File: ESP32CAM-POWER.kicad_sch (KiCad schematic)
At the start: 20 parts

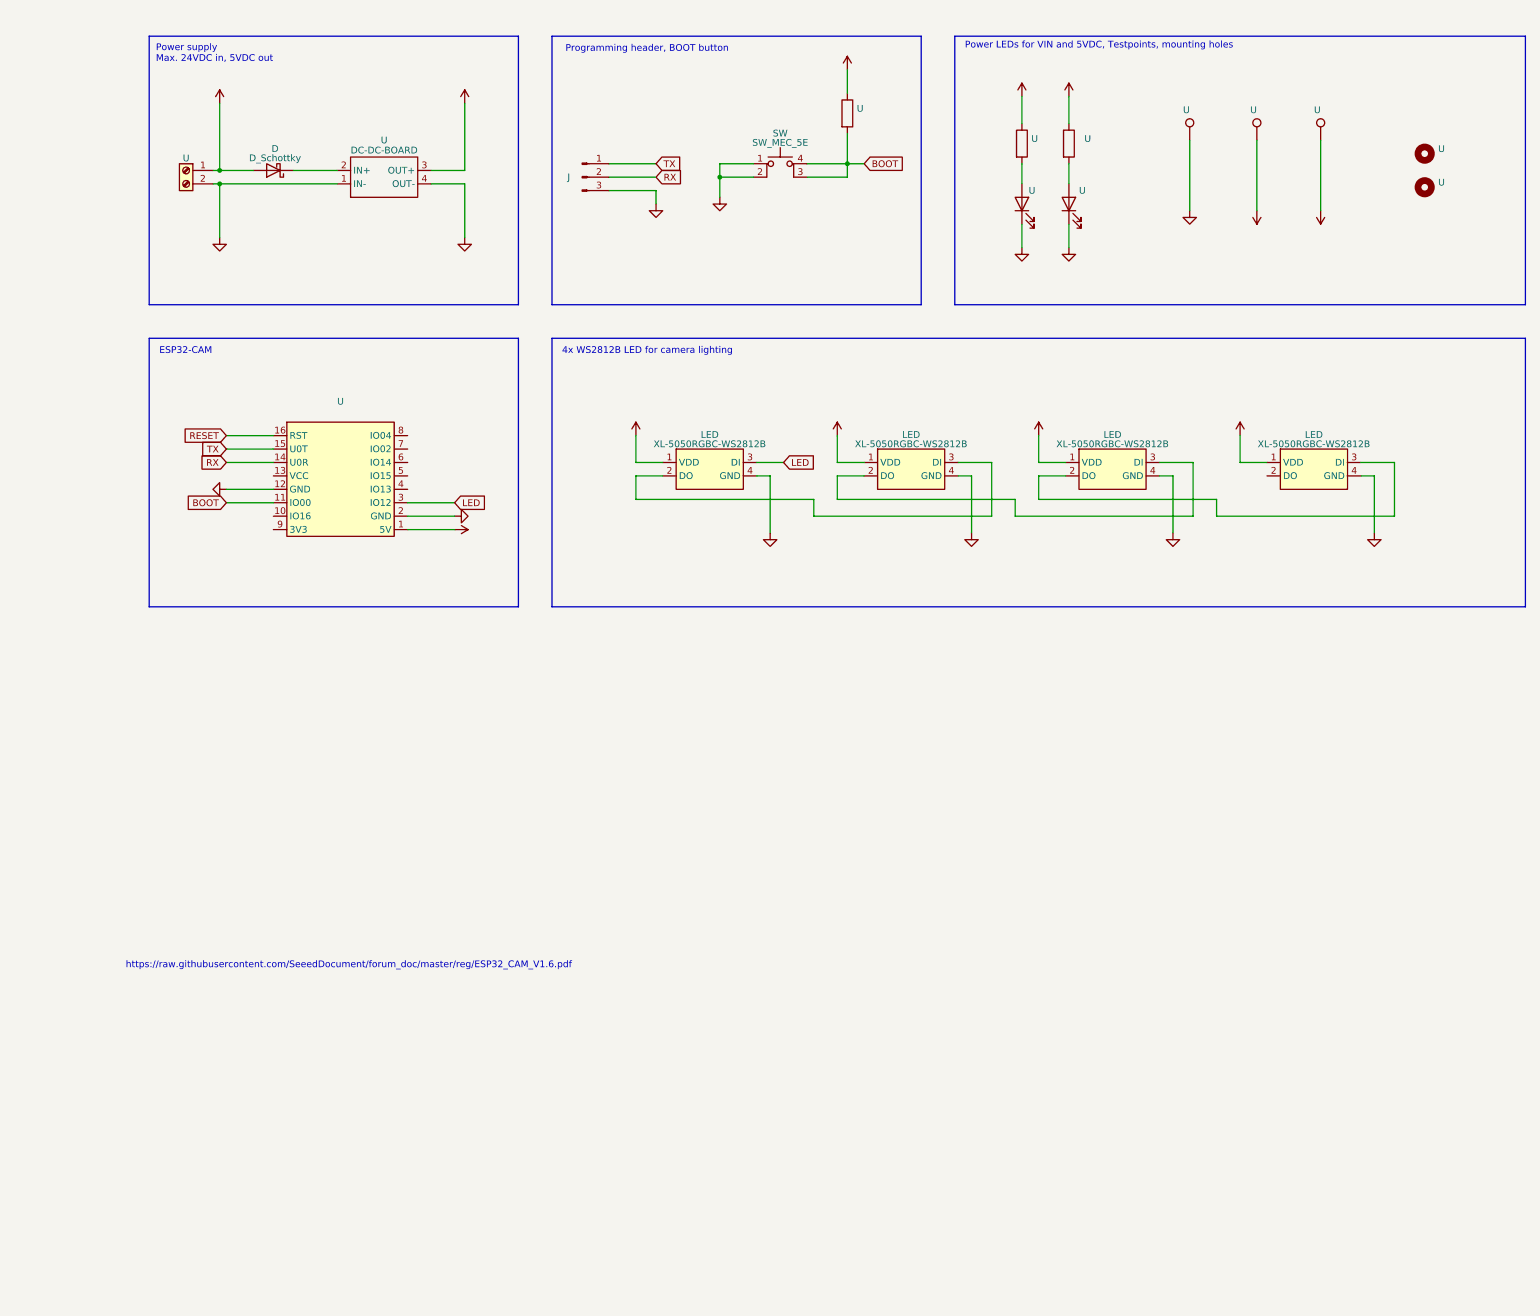
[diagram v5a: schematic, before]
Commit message: fixed several bugs, replaced DCDC Module with onboard step down
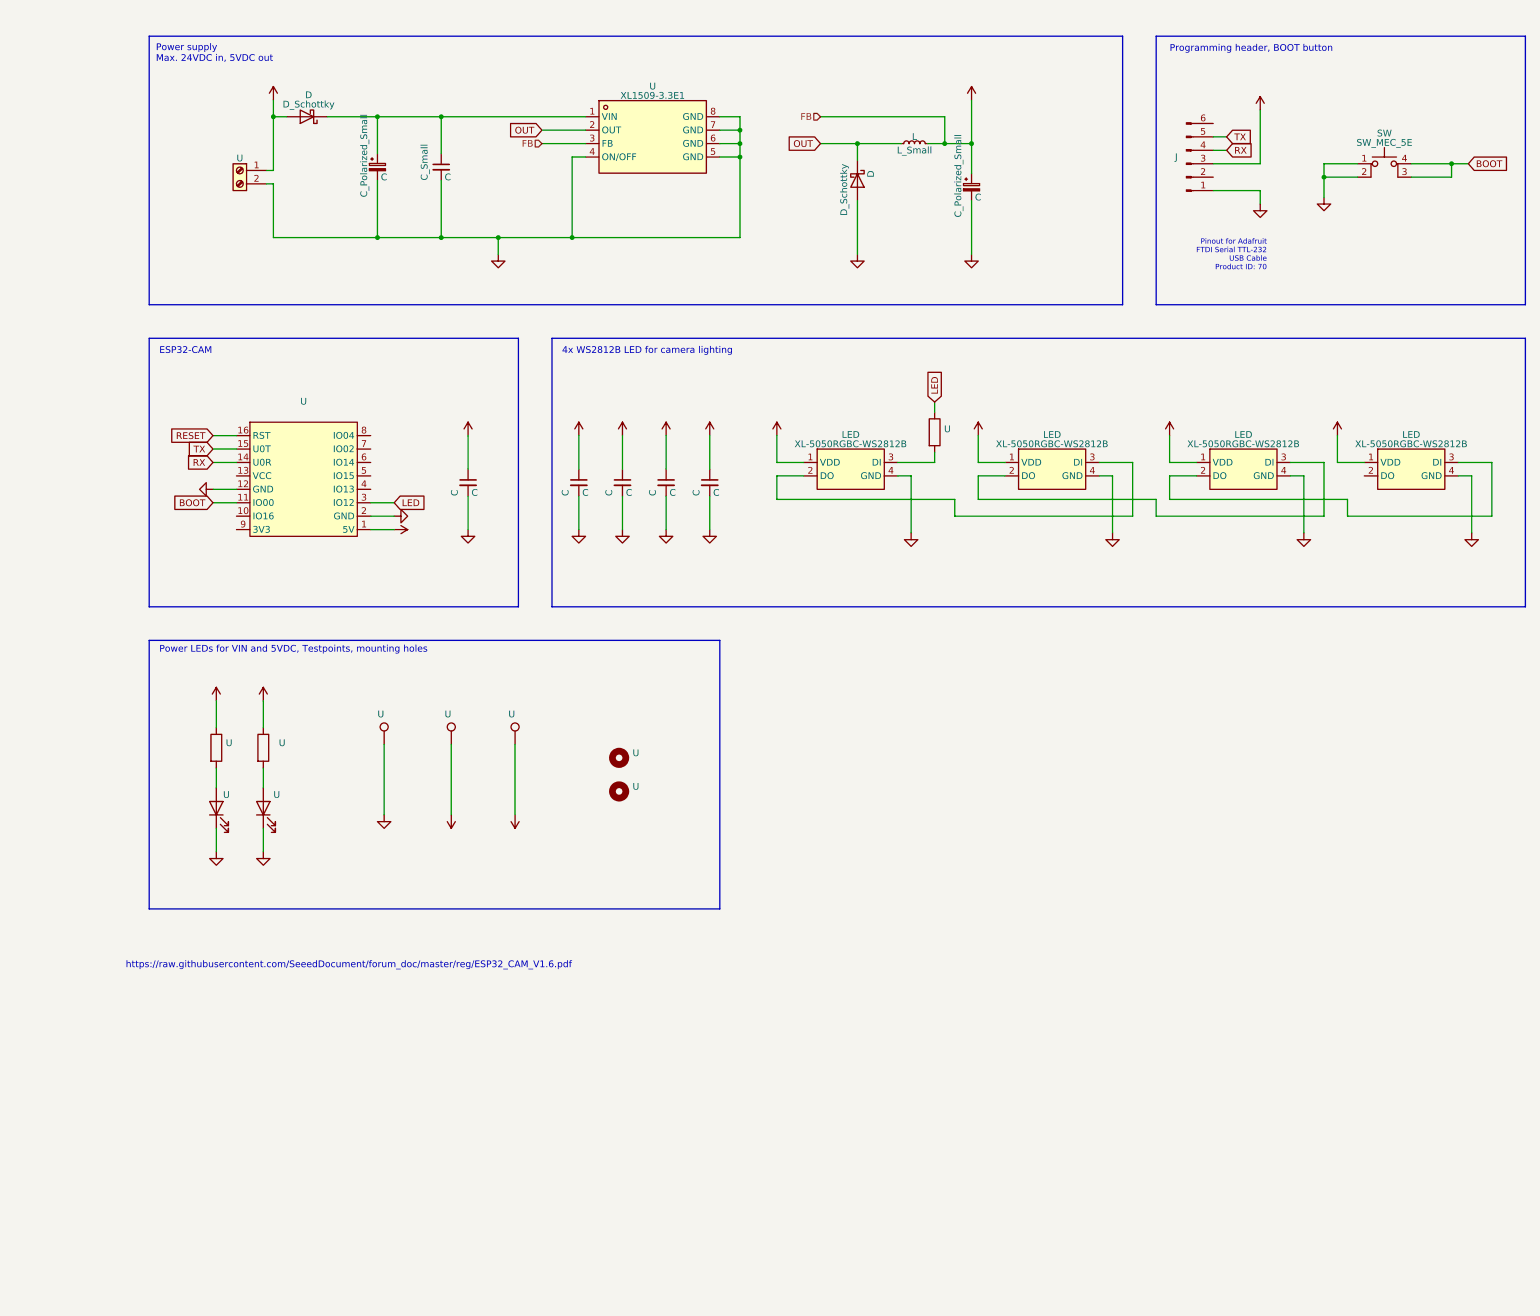
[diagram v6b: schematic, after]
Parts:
- removed J: Conn_01x03_Male, symbol Connector:Conn_01x03_Male
- removed U: DC-DC-BOARD, symbol bouni:DC-DC-BOARD
- added C (x5): C, symbol Device:C_Small
- added C: C_Small, symbol Device:C_Small
- added C (x2): C_Polarized_Small, symbol Device:C_Polarized_Small
- added D: D_Schottky, symbol Device:D_Schottky
- added J: Conn_01x06_Male, symbol Connector:Conn_01x06_Male
- added L: L_Small, symbol Device:L_Small
- added U: XL1509-3.3E1, SOP-8_L4.9-W3.9-P1.27-LS6.0-BL, symbol LCSC:XL1509-3.3E1
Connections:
- net +5V: now also C.1, C.1, C.1, C.1, C.1, C.1, J.3 (Pin_3), L.2, U.3 (FB); no longer U.1
- net BOOT: no longer U.2
- net GND: now also C.2, C.2, C.2, C.2, C.2, C.2, C.2, C.2, D.2 (A), J.1 (Pin_1), U.4 (ON/OFF), U.5 (GND), U.6 (GND), U.7 (GND), U.8 (GND)
- net LED: now also U.1; no longer LED.3 (DI)
- net RX: now also J.4 (Pin_4)
- net TX: now also J.5 (Pin_5)
- net at D.1 (K): now also C.1, C.1, U.1 (VIN)
- new net: LED.3 (DI), U.2
- new net OUT: D.1 (K), L.1, U.2 (OUT)
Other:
- note added: "Pinout for Adafruit FTDI Serial TTL-232 USB Cable Product ID: 70"
- moved on the sheet: D, LED, SW, U

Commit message: last cleanups
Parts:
- C, D, SW, U: JLC Part (none) -> Basic Part
- C: JLC Part (none) -> Extended Part
- LED: LCSC (none) -> C2843785; LCSC Part C2843785 -> (none)
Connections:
- net VIN: now reaches C.1, C.1, D.1 (K), U.1 (VIN)
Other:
- note added: "Pinout for Adafruit FTDI Serial TTL-232 USB Cable Product ID: 70 Compatible with FTDI TTL-232R-*"
- note removed: "Pinout for Adafruit FTDI Serial TTL-232 USB Cable Product ID: 70"
- moved on the sheet: C, D, L, U

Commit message: Ooctober 2024 Update
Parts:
- removed C: C_Small, symbol Device:C_Small
- removed C (x2): C_Polarized_Small, symbol Device:C_Polarized_Small
- removed D (x2): D_Schottky, symbol Device:D_Schottky
- removed J: Conn_01x06_Male, symbol Connector:Conn_01x06_Male
- removed L: L_Small, symbol Device:L_Small
- removed SW: SW_MEC_5E, symbol Switch:SW_MEC_5E
- removed U: XL1509-3.3E1, SOP-8_L4.9-W3.9-P1.27-LS6.0-BL, symbol LCSC:XL1509-3.3E1
- added C6: 0.1uF, Capacitor_SMD:C_0402_1005Metric, symbol Device:C_Small
- added C7: 100uF, Capacitor_SMD:CP_Elec_6.3x5.8, symbol Device:C_Polarized_Small
- added D3: 1N5819WS, Diode_SMD:D_SOD-323, symbol Diode:1N5819WS
- added J2: USB_C_Receptacle_USB2.0_16P, LCSC:USB-C-SMD_TYPE-C-6PIN-2MD-073, symbol Connector:USB_C_Receptacle_USB2.0_16P
- added PS1: TSR_1-2450SM, TSR124120SM, symbol TSR_1-2450SM:TSR_1-2450SM
- added R4, R5: 5K1, Resistor_SMD:R_0603_1608Metric, symbol Device:R
- added SW1, SW2: SW_Omron_B3S, Button_Switch_SMD:SW_SPST_B3S-1000, symbol Switch:SW_Omron_B3FS
- added U1: CH340X, Package_SO:MSOP-10_3x3mm_P0.5mm, symbol Interface_USB:CH340X
- C1, C2, C3, C4, C5: renamed from C; value C -> 0.1uF; footprint (none) -> Capacitor_SMD:C_0402_1005Metric; LCSC C14663 -> C1525
- D1: renamed from U; value (none) -> LED_B; footprint (none) -> LED_SMD:LED_0603_1608Metric; LCSC C72038 -> C965807
- D2: renamed from U; value (none) -> LED_G; footprint (none) -> LED_SMD:LED_0603_1608Metric; LCSC C72043 -> C965804
- H1, H2: renamed from U; value (none) -> MountingHole; footprint (none) -> MountingHole:MountingHole_3.2mm_M3_ISO14580; now not fitted
- J1: renamed from U; value (none) -> Screw_Terminal_01x02; footprint (none) -> SPTAF1:1861933; now not fitted
- LED1, LED2, LED3, LED4: renamed from LED; value XL-5050RGBC-WS2812B -> XL-1010RGBC-WS2812B; footprint LED-SMD_4P-L5.0-W5.0-BL_XL-5050RGBC -> LCSC:LED-SMD_4P-L1.0-W1.0-TL_XL-1010RGBC-WS2812B; symbol LCSC:XL-5050RGBC-WS2812B -> XL-1010RGBC-WS2812B:XL-1010RGBC-WS2812B; LCSC C2843785 -> C5349953
- R1: renamed from U; value (none) -> 10k; footprint (none) -> Resistor_SMD:R_0603_1608Metric
- R2: renamed from U; value (none) -> 680; footprint (none) -> Resistor_SMD:R_0603_1608Metric
- R3: renamed from U; value (none) -> 470; footprint (none) -> Resistor_SMD:R_0603_1608Metric; LCSC C25804 -> C23179
- TP1, TP2, TP3: renamed from U; value (none) -> TestPoint; footprint (none) -> TestPoint:TestPoint_Pad_D1.5mm; now not fitted
- U2: renamed from U; value (none) -> ESP32-CAM; footprint (none) -> bouni:ESP32-CAM; now not fitted
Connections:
- net +5V: now also LED1.2 (VDD), LED2.2 (VDD), LED3.2 (VDD), LED4.2 (VDD), C7.1, D3.1 (K), PS1.5 (+VOUT), U1.7 (VCC); no longer LED1.1 (VDD), LED2.1 (VDD), LED3.1 (VDD), LED4.1 (VDD)
- net BOOT: now also SW1.2
- net GND: now also LED1.3 (GND), LED2.3 (GND), LED3.3 (GND), LED4.3 (GND), C6.1, C7.2, J2.A1 (GND), J2.A12 (GND), J2.B1 (GND), J2.B12 (GND), PS1.7 (GND_1), PS1.9 (GND_2), R4.2, R5.2, SW1.1, SW2.1, U1.3 (GND); no longer LED1.4 (GND), LED2.4 (GND), LED3.4 (GND), LED4.4 (GND)
- net RESET: now also SW2.2
- net VCC: now also PS1.1 (+VIN)
- net at R3.2: now also LED1.4 (DIN); no longer LED1.3 (DI)
- net RX renamed TXD
- net TXD: now also U1.8 (TXD)
- net TX renamed RXD
- net RXD: now also U1.9 (RXD)
- new net: C6.2, U1.10 (V3)
- new net: D3.2 (A), J2.A4 (VBUS), J2.A9 (VBUS), J2.B4 (VBUS), J2.B9 (VBUS)
- new net: J2.A5 (CC1), R4.1
- new net: J2.B5 (CC2), R5.1
- new net D+: J2.A6 (D+), J2.B6 (D+), U1.1 (UD+)
- new net D-: J2.A7 (D-), J2.B7 (D-), U1.2 (UD-)
- new net D1: LED1.1 (DOUT), LED2.4 (DIN)
- new net D2: LED2.1 (DOUT), LED3.4 (DIN)
- new net D3: LED3.1 (DOUT), LED4.4 (DIN)
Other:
- note removed: "Pinout for Adafruit FTDI Serial TTL-232 USB Cable Product ID: 70 Compatible with FTDI TTL-232R-*"
- note removed: "Programming header, BOOT button"
- moved on the sheet: R3
